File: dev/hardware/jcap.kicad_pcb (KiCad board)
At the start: 2 copper layers, 140 x 87 mm, 74 parts, among them J201 CPU PGMR, J202 GPU PGMR, J203 SPARE GPU HDR, J204 SPARE CPU HDR, J301 DC IN, J502 VGA OUT, J601 CONTROLS, SW201 CPU ~{RES}, SW202 GPU ~{RES}, SW203 DEBUG, SW601 TILT, U101 P8X32A-D40, U201 P8X32A-D40, U302 LF33_TO220, U401 24LC256, U402 24LC256, U601 74HC165, U602 74HC165, Y101 6.5MHz, Y201 6.5MHz

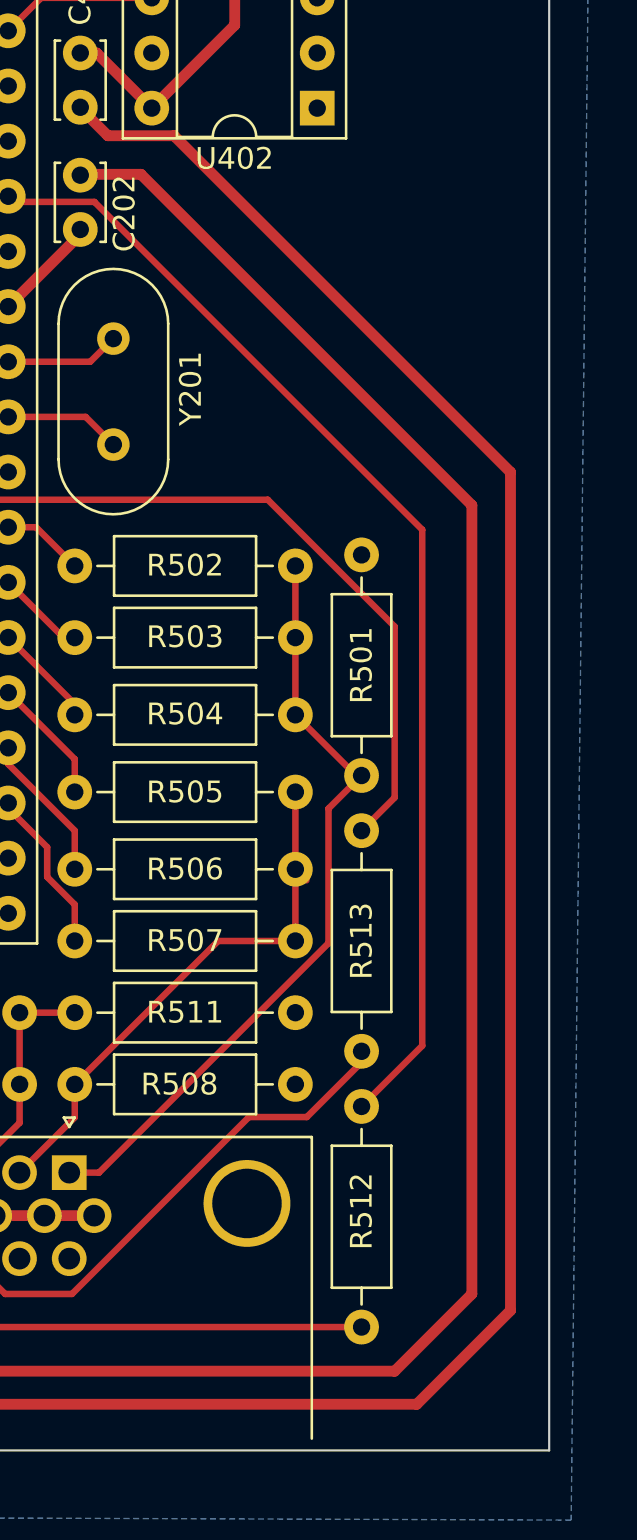
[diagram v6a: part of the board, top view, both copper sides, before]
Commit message: Updated input header pinout
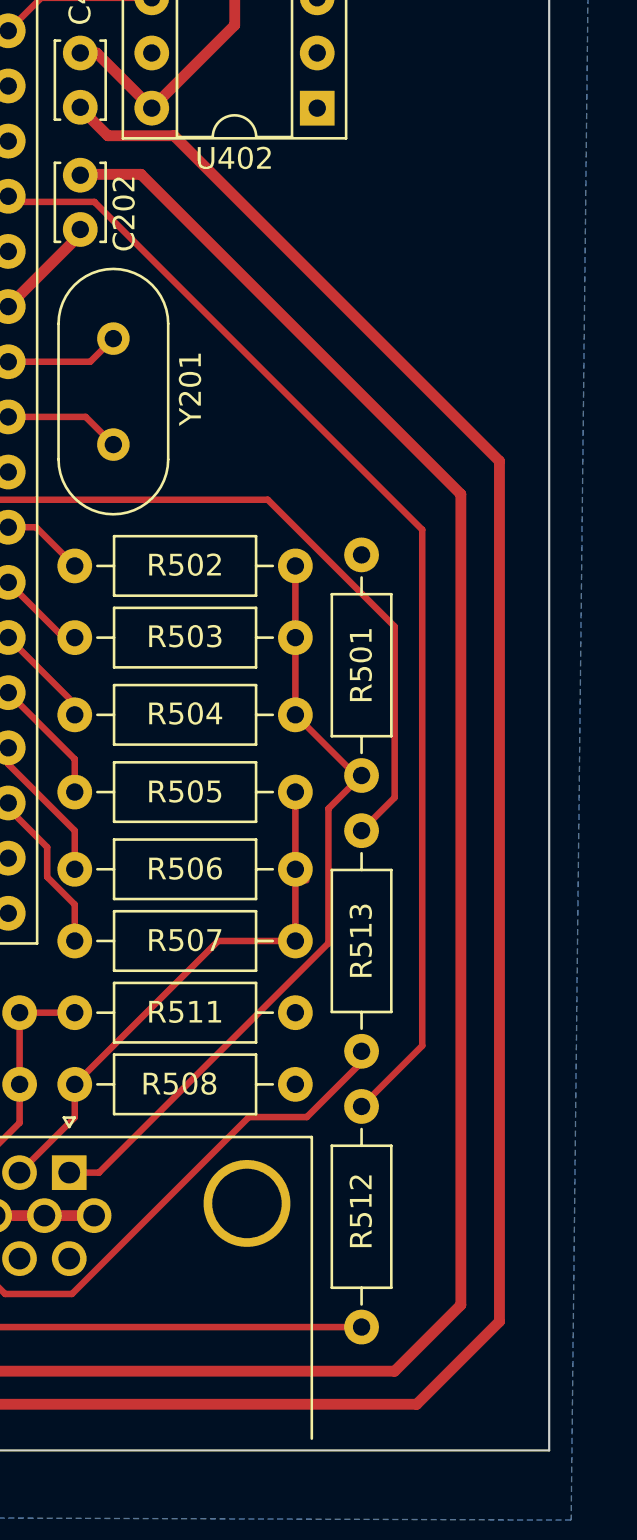
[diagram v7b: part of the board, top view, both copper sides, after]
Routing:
- net +3.3V: track 838.7 -> 837.9 mm
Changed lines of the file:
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@@
     (effects (font (size 1 1) (thickness 0.15)))
   )
-  (segment (start 203.2 94.234) (end 218.44 109.474) (width 0.5) (layer "F.Cu") (net 1))
   (segment (start 115.276 75.184) (end 117.856 75.184) (width 0.5) (layer "F.Cu") (net 1))
-  (segment (start 200.406 93.98) (end 200.66 94.234) (width 0.5) (layer "F.Cu") (net 1))
   (segment (start 147.828 135.168) (end 150.114 137.454) (width 0.5) (layer "F.Cu") (net 1))
+  (segment (start 151.638 150.876) (end 150.114 149.352) (width 0.5) (layer "F.Cu") (net 1))
   (segment (start 88.392 134.112) (end 88.392 137.414) (width 0.5) (layer "F.Cu") (net 1))
   (segment (start 143.256 134.874) (end 145.796 137.414) (width 0.5) (layer "F.Cu") (net 1))
-  (segment (start 215.9 150.876) (end 151.638 150.876) (width 0.5) (layer "F.Cu") (net 1))
+  (segment (start 214.884 149.352) (end 150.114 149.352) (width 0.5) (layer "F.Cu") (net 1))
   (segment (start 139.455767 106.69) (end 147.828 115.062233) (width 0.5) (layer "F.Cu") (net 1))
-  (segment (start 200.406 91.186) (end 201.676 92.456) (width 0.5) (layer "F.Cu") (net 1))
   (segment (start 135.636 102.91) (end 137.16 104.434) (width 0.5) (layer "F.Cu") (net 1))
   (segment (start 166.624 138.938) (end 166.624 114.626) (width 0.5) (layer "F.Cu") (net 1))
+  (segment (start 201.676 92.456) (end 204.724 92.456) (width 0.5) (layer "F.Cu") (net 1))
   (segment (start 153.406 96.53) (end 152.4 97.536) (width 0.5) (layer "F.Cu") (net 1))
-  (segment (start 220.218 146.558) (end 215.9 150.876) (width 0.5) (layer "F.Cu") (net 1))
-  (segment (start 151.638 150.876) (end 150.114 149.352) (width 0.5) (layer "F.Cu") (net 1))
   (segment (start 156.25 96.53) (end 153.406 96.53) (width 0.5) (layer "F.Cu") (net 1))
   (segment (start 152.146 142.982) (end 151.15 141.986) (width 0.5) (layer "F.Cu") (net 1))
   (segment (start 122.936 90.932) (end 122.936 123.444) (width 0.5) (layer "F.Cu") (net 1))
-  (segment (start 218.44 145.796) (end 214.884 149.352) (width 0.5) (layer "F.Cu") (net 1))
-  (segment (start 218.44 109.474) (end 218.44 145.796) (width 0.5) (layer "F.Cu") (net 1))
   (segment (start 115.276 118.374) (end 113.996 119.654) (width 0.5) (layer "F.Cu") (net 1))
   (segment (start 157.51 92.72) (end 156.24 93.99) (width 0.5) (layer "F.Cu") (net 1))
   (segment (start 166.624 114.626) (end 175.26 105.99) (width 0.5) (layer "F.Cu") (net 1))
+  (segment (start 203.2 94.234) (end 217.932 108.966) (width 0.5) (layer "F.Cu") (net 1))
   (segment (start 150.114 97.028) (end 150.114 137.454) (width 0.5) (layer "F.Cu") (net 1))
   (segment (start 122.936 123.444) (end 122.936 137.668) (width 0.5) (layer "F.Cu") (net 1))
-  (segment (start 204.724 92.456) (end 220.218 107.95) (width 0.5) (layer "F.Cu") (net 1))
   (segment (start 170.688 114.046233) (end 178.562 106.172233) (width 0.5) (layer "F.Cu") (net 1))
   (segment (start 155.956 143.256) (end 166.116 143.256) (width 0.5) (layer "F.Cu") (net 1))
   (segment (start 142.494 143.256) (end 148.59 149.352) (width 0.5) (layer "F.Cu") (net 1))
   (segment (start 147.828 140.716) (end 147.828 139.74) (width 0.5) (layer "F.Cu") (net 1))
+  (segment (start 200.66 94.234) (end 203.2 94.234) (width 0.5) (layer "F.Cu") (net 1))
   (segment (start 147.828 139.74) (end 150.114 137.454) (width 0.5) (layer "F.Cu") (net 1))
   (segment (start 164.592 140.97) (end 166.624 138.938) (width 0.5) (layer "F.Cu") (net 1))
+  (segment (start 219.71 147.066) (end 215.9 150.876) (width 0.5) (layer "F.Cu") (net 1))
   (segment (start 88.392 80.264) (end 88.392 90.932) (width 0.5) (layer "F.Cu") (net 1))
   (segment (start 147.828 115.062233) (end 147.828 135.168) (width 0.5) (layer "F.Cu") (net 1))
@@
   (segment (start 135.646 102.88) (end 135.646 102.87) (width 0.5) (layer "F.Cu") (net 1))
   (segment (start 152.4 97.536) (end 152.4 135.168) (width 0.5) (layer "F.Cu") (net 1))
-  (segment (start 220.218 107.95) (end 220.218 146.558) (width 0.5) (layer "F.Cu") (net 1))
   (segment (start 157.49 95.29) (end 156.25 96.53) (width 0.5) (layer "F.Cu") (net 1))
   (segment (start 88.392 90.932) (end 88.392 123.444) (width 0.5) (layer "F.Cu") (net 1))
@@
   (segment (start 150.154 137.454) (end 155.956 143.256) (width 0.5) (layer "F.Cu") (net 1))
   (segment (start 145.796 137.414) (end 150.074 137.414) (width 0.5) (layer "F.Cu") (net 1))
-  (segment (start 200.406 91.146) (end 200.406 91.186) (width 0.5) (layer "F.Cu") (net 1))
   (segment (start 152.4 135.168) (end 150.114 137.454) (width 0.5) (layer "F.Cu") (net 1))
   (segment (start 150.114 137.454) (end 154.98 137.454) (width 0.5) (layer "F.Cu") (net 1))
   (segment (start 138.186 106.69) (end 139.455767 106.69) (width 0.5) (layer "F.Cu") (net 1))
   (segment (start 158.496 140.97) (end 164.592 140.97) (width 0.5) (layer "F.Cu") (net 1))
-  (segment (start 214.884 149.352) (end 150.114 149.352) (width 0.5) (layer "F.Cu") (net 1))
   (segment (start 149.098 141.986) (end 147.828 140.716) (width 0.5) (layer "F.Cu") (net 1))
   (segment (start 178.562 106.172233) (end 178.562 105.44) (width 0.5) (layer "F.Cu") (net 1))
   (segment (start 153.152 93.99) (end 150.114 97.028) (width 0.5) (layer "F.Cu") (net 1))
+  (segment (start 200.406 91.146) (end 200.406 91.186) (width 0.5) (layer "F.Cu") (net 1))
   (segment (start 88.392 137.414) (end 101.854 150.876) (width 0.5) (layer "F.Cu") (net 1))
-  (segment (start 200.66 94.234) (end 203.2 94.234) (width 0.5) (layer "F.Cu") (net 1))
   (segment (start 122.936 134.112) (end 126.238 137.414) (width 0.5) (layer "F.Cu") (net 1))
   (segment (start 156.24 93.99) (end 153.152 93.99) (width 0.5) (layer "F.Cu") (net 1))
   (segment (start 113.996 119.654) (end 108.956233 119.654) (width 0.5) (layer "F.Cu") (net 1))
+  (segment (start 217.932 146.304) (end 214.884 149.352) (width 0.5) (layer "F.Cu") (net 1))
   (segment (start 112.014 143.256) (end 142.494 143.256) (width 0.5) (layer "F.Cu") (net 1))
   (segment (start 106.172 137.414) (end 112.014 143.256) (width 0.5) (layer "F.Cu") (net 1))
   (segment (start 148.59 149.352) (end 150.114 149.352) (width 0.5) (layer "F.Cu") (net 1))
+  (segment (start 200.406 93.98) (end 200.66 94.234) (width 0.5) (layer "F.Cu") (net 1))
   (segment (start 154.98 137.454) (end 158.496 140.97) (width 0.5) (layer "F.Cu") (net 1))
   (segment (start 88.392 123.444) (end 88.392 134.112) (width 0.5) (layer "F.Cu") (net 1))
-  (segment (start 201.676 92.456) (end 204.724 92.456) (width 0.5) (layer "F.Cu") (net 1))
   (segment (start 150.074 137.414) (end 150.114 137.454) (width 0.5) (layer "F.Cu") (net 1))
   (segment (start 126.238 137.414) (end 145.796 137.414) (width 0.5) (layer "F.Cu") (net 1))
+  (segment (start 219.71 107.442) (end 219.71 147.066) (width 0.5) (layer "F.Cu") (net 1))
   (segment (start 166.116 143.256) (end 170.688 138.684) (width 0.5) (layer "F.Cu") (net 1))
   (segment (start 137.16 104.434) (end 137.16 105.664) (width 0.5) (layer "F.Cu") (net 1))
+  (segment (start 215.9 150.876) (end 151.638 150.876) (width 0.5) (layer "F.Cu") (net 1))
   (segment (start 151.15 141.986) (end 149.098 141.986) (width 0.5) (layer "F.Cu") (net 1))
   (segment (start 150.114 137.454) (end 150.154 137.454) (width 0.5) (layer "F.Cu") (net 1))
@@
   (segment (start 101.854 150.876) (end 148.59 150.876) (width 0.5) (layer "F.Cu") (net 1))
   (segment (start 150.114 149.352) (end 152.146 147.32) (width 0.5) (layer "F.Cu") (net 1))
+  (segment (start 217.932 108.966) (end 217.932 146.304) (width 0.5) (layer "F.Cu") (net 1))
   (segment (start 137.16 105.664) (end 138.186 106.69) (width 0.5) (layer "F.Cu") (net 1))
   (segment (start 106.172 122.438233) (end 106.172 137.414) (width 0.5) (layer "F.Cu") (net 1))
+  (segment (start 204.724 92.456) (end 219.71 107.442) (width 0.5) (layer "F.Cu") (net 1))
+  (segment (start 200.406 91.186) (end 201.676 92.456) (width 0.5) (layer "F.Cu") (net 1))
   (segment (start 181.844 107.94) (end 181.849 107.945) (width 0.5) (layer "F.Cu") (net 2))
   (segment (start 178.562 107.94) (end 181.844 107.94) (width 0.5) (layer "F.Cu") (net 2))

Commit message: Finalized optimized board layout
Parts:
- removed R201, R202, R205, R206, R207, R208, R209, R210: 200, Resistor_THT:R_Axial_DIN0207_L6.3mm_D2.5mm_P10.16mm_Horizontal
- removed R609, R610, R611, R612, R613, R614, R615, R616, R618, R619, R620, R621, R622, R623, R624, R625: 10K, Resistor_THT:R_Axial_DIN0207_L6.3mm_D2.5mm_P10.16mm_Horizontal
- added RN601: 10K, Resistor_THT:R_Array_SIP9, F.Cu at (124.2, 105.2)
- added RN602: 10K, Resistor_THT:R_Array_SIP9, F.Cu at (124.2, 115.3)
- moved R203 32.8 mm to (156.7, 68.8), turned to 0 degrees
- moved SW203 27.6 mm to (159.8, 77.0), turned to 0 degrees
- moved J301 27.2 mm to (163.1, 140.3)
- moved R204 24.1 mm to (166.9, 72.1), turned to 180 degrees
- moved SW201 23.9 mm to (131.7, 70.6)
- moved C602 22.2 mm to (116.9, 140.2)
- moved R617 17.9 mm to (128.3, 146.6)
- moved J203 17.7 mm to (164.6, 96.5)
- moved SW601 17.5 mm to (130.2, 131.7), turned to -90 degrees
- moved R301 16.5 mm to (128.3, 141.7), turned to 0 degrees
- moved C301 14.9 mm to (159.8, 136.1), turned to 180 degrees
- moved U302 11.6 mm to (153.2, 133.1), turned to 180 degrees
- moved U602 11.2 mm to (109.2, 83.6)
- moved C601 11.0 mm to (119.9, 83.6), turned to -90 degrees
- moved C302 9.91 mm to (157.3, 133.1), turned to 0 degrees
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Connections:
- U101 pad 21: /Propellers/CPU_DAT_8 -> /Propellers/GFX_DAT_8
- U101 pad 22: /Propellers/CPU_DAT_7 -> /Propellers/GFX_DAT_7
- U101 pad 23: /Propellers/CPU_DAT_6 -> /Propellers/GFX_DAT_6
- U101 pad 24: /Propellers/CPU_DAT_5 -> /Propellers/GFX_DAT_5
- U101 pad 25: /Propellers/CPU_DAT_4 -> /Propellers/GFX_DAT_4
- U101 pad 26: /Propellers/CPU_DAT_3 -> /Propellers/GFX_DAT_3
- U101 pad 27: /Propellers/CPU_DAT_2 -> /Propellers/GFX_DAT_2
- U101 pad 28: /Propellers/CPU_DAT_1 -> /Propellers/GFX_DAT_1
- U201 pad 13: /Propellers/GPU_DAT_1 -> /Propellers/GFX_DAT_1
- U201 pad 14: /Propellers/GPU_DAT_2 -> /Propellers/GFX_DAT_2
- U201 pad 15: /Propellers/GPU_DAT_3 -> /Propellers/GFX_DAT_3
- U201 pad 16: /Propellers/GPU_DAT_4 -> /Propellers/GFX_DAT_4
- U201 pad 17: /Propellers/GPU_DAT_5 -> /Propellers/GFX_DAT_5
- U201 pad 18: /Propellers/GPU_DAT_6 -> /Propellers/GFX_DAT_6
- U201 pad 19: /Propellers/GPU_DAT_7 -> /Propellers/GFX_DAT_7
- U201 pad 20: /Propellers/GPU_DAT_8 -> /Propellers/GFX_DAT_8
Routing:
- net +3.3V: track 837.9 -> 635.1 mm
- net ~{INPUTS_PL}: track 138.4 -> 87.4 mm
- net /Propellers/DEBUG: track 75.9 -> 33.8 mm
- net INPUTS_CLK: track 130.0 -> 105.6 mm
- net Net-(U601-VCC): track 3.31 -> 26.9 mm
- net /Propellers/GFX_DAT_1: track 0.00 -> 20.7 mm
- net /Input/SHIFT_IN: track 66.9 -> 46.3 mm
- net Net-(U601-DS): track 15.7 -> 35.9 mm
- net /Propellers/GFX_DAT_8: track 0.00 -> 19.8 mm
- net /Propellers/GFX_DAT_7: track 0.00 -> 19.8 mm
- net /Propellers/GFX_DAT_5: track 0.00 -> 19.8 mm
- net /Propellers/GFX_DAT_4: track 0.00 -> 19.8 mm
- net /Propellers/GFX_DAT_2: track 0.00 -> 19.8 mm
- net /Propellers/GFX_DAT_6: track 0.00 -> 19.8 mm
- net /Propellers/GFX_DAT_3: track 0.00 -> 19.8 mm
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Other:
- board size 140 x 87 mm -> 115.6 x 87 mm
